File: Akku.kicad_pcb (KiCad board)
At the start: 2 copper layers, 100 x 160 mm, 34 parts, among them P1 CONN_02X10, P2 CONN_02X10, P3 CONN_02X10, SW1 SWITCH_INV, SW2 SWITCH_INV, SW3 SWITCH_INV, U4 74LS193, U5 74LS541, U6 74LS193, U7 74LS540

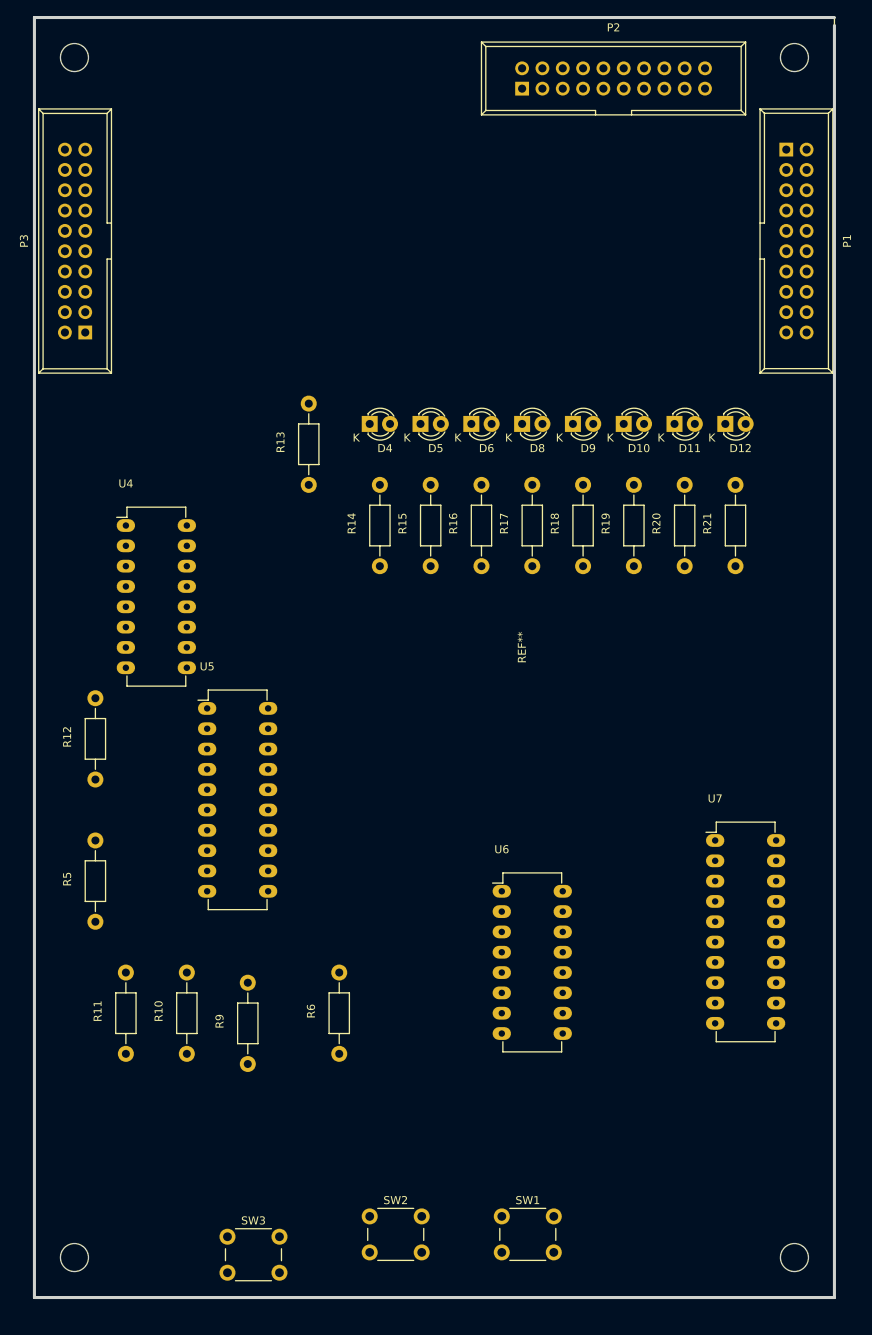
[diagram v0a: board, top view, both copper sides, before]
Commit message: Akku/PC PCB verbessert
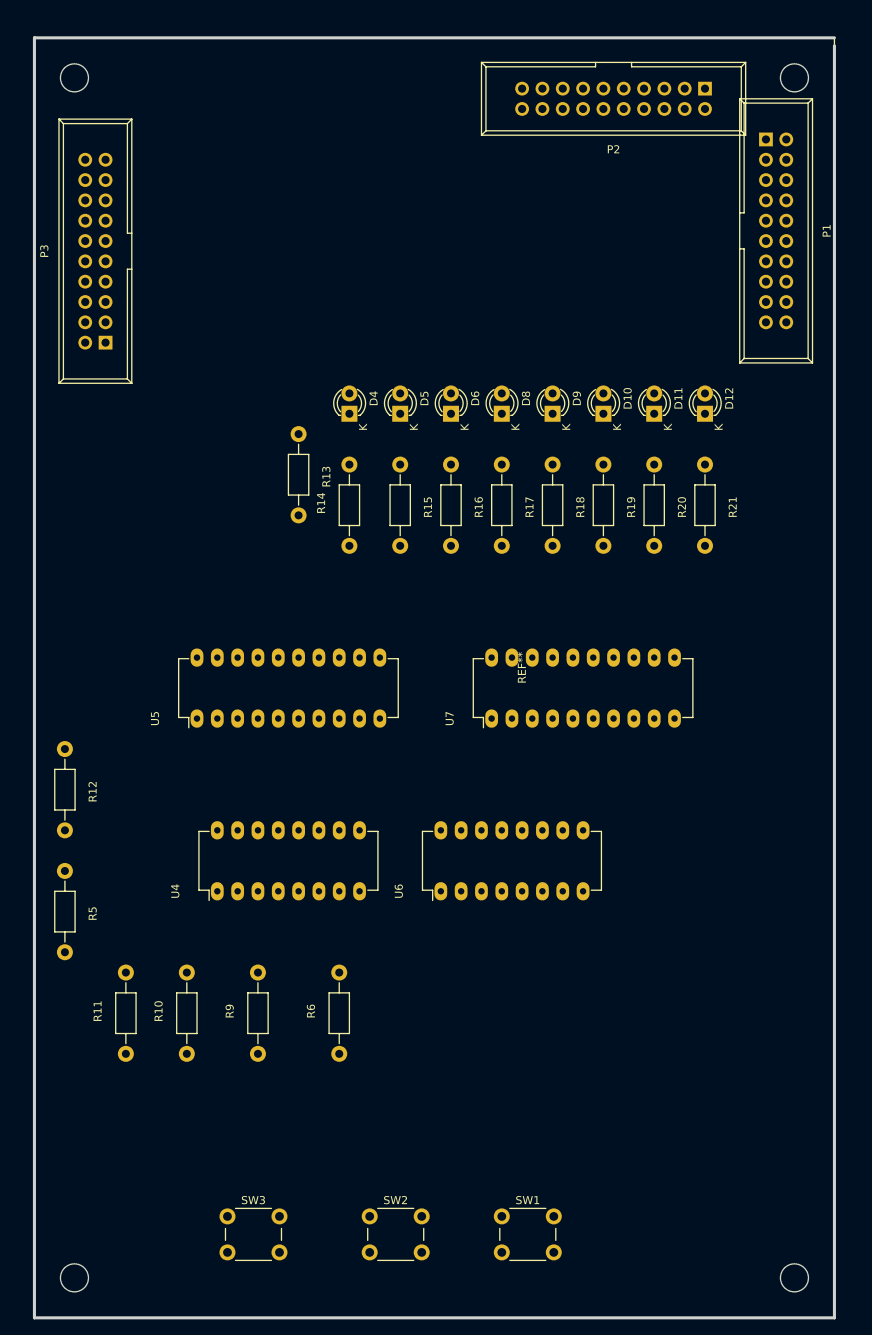
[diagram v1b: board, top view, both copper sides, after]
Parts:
- moved U4 47.1 mm to (73.7, 163.8), turned to 90 degrees
- moved U7 31.8 mm to (108.0, 142.2), turned to 90 degrees
- moved P2 22.9 mm to (134.6, 63.5), turned to 180 degrees
- moved R15 13.3 mm to (96.5, 110.5), turned to 270 degrees
- moved R16 13.3 mm to (102.9, 110.5), turned to 270 degrees
- moved R17 13.3 mm to (109.2, 110.5), turned to 270 degrees
- moved R18 13.3 mm to (115.6, 110.5), turned to 270 degrees
- moved R19 13.3 mm to (121.9, 110.5), turned to 270 degrees
- moved R20 13.3 mm to (128.3, 110.5), turned to 270 degrees
- moved R21 13.3 mm to (134.6, 110.5), turned to 270 degrees
- moved U6 7.62 mm to (101.6, 163.8), turned to 90 degrees
- moved R5 7.41 mm to (54.6, 161.3), turned to 270 degrees
- moved R13 6.48 mm to (83.8, 106.7), turned to 270 degrees
- moved R12 5.39 mm to (54.6, 146.1), turned to 270 degrees
- moved R14 4.58 mm to (90.2, 120.7)
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
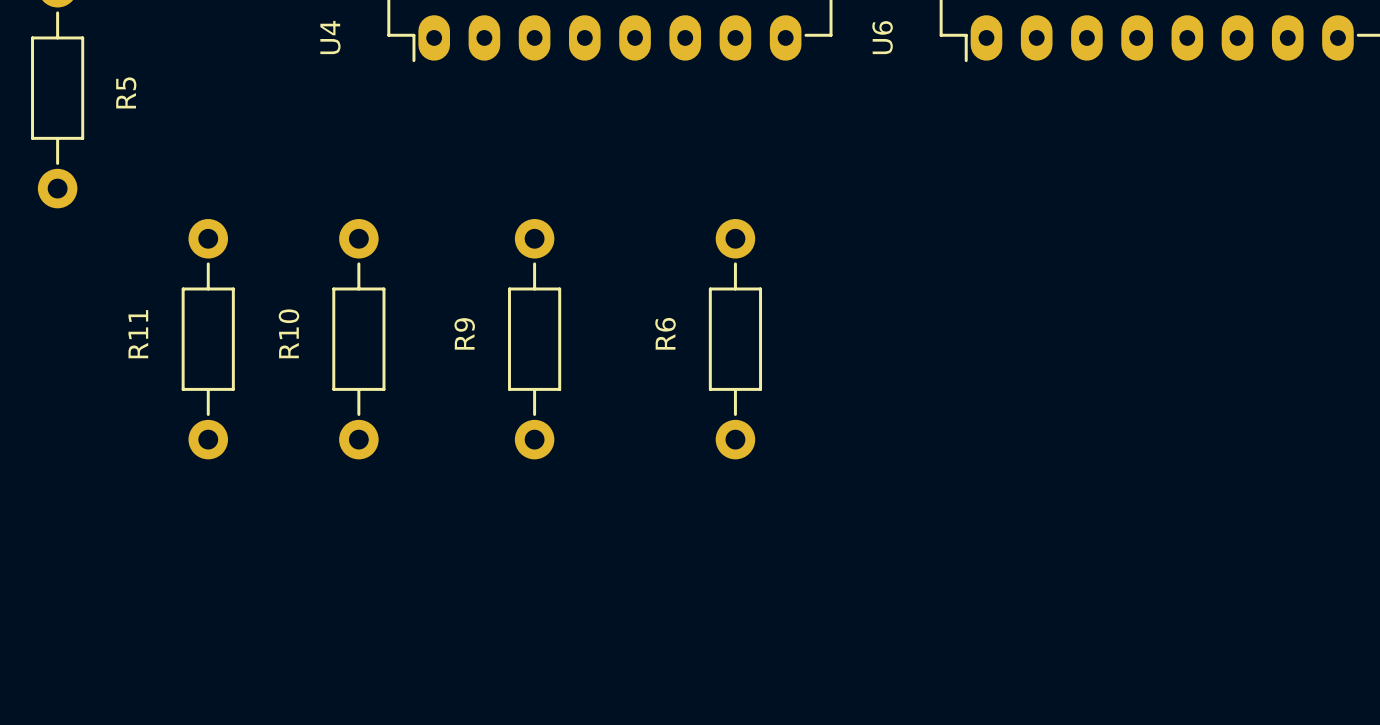
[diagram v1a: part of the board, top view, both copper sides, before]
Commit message: Fehler am Schaltplan ausgebessert; PCB erweitert
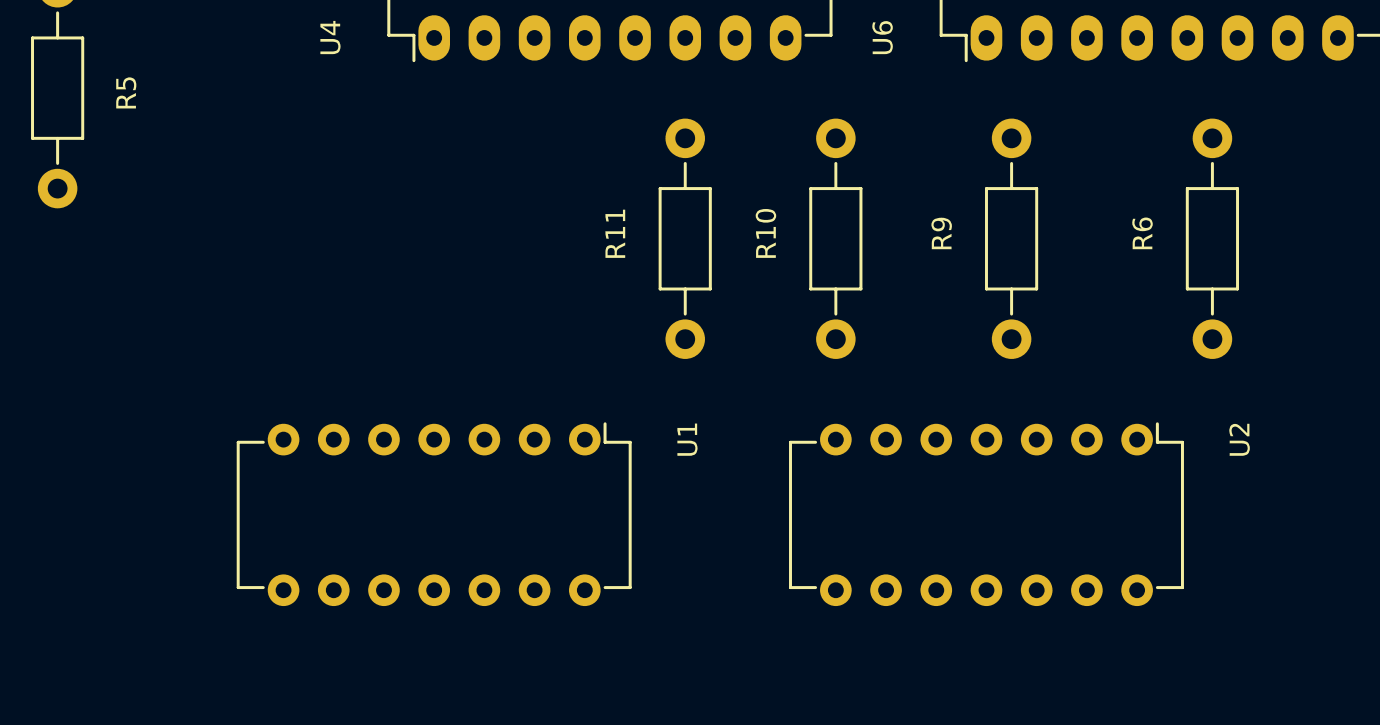
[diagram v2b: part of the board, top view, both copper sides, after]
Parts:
- added U1: 7400, Housings_DIP:DIP-14_W7.62mm, F.Cu at (81.3, 184.2)
- added U2: 7408, Housings_DIP:DIP-14_W7.62mm, F.Cu at (109.2, 184.2)
- moved R10 24.7 mm to (94.0, 179.1)
- moved R9 24.7 mm to (102.9, 179.1)
- moved R11 24.7 mm to (86.4, 179.1)
- moved R6 24.7 mm to (113.0, 179.1)

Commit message: netzlisten neu
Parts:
- moved P1 28.2 mm to (146.1, 97.8), turned to 90 degrees
- moved P2 25.5 mm to (109.2, 66.0), turned to 0 degrees
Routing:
- net Net-(P1-Pad1): track 0.00 -> 27.9 mm
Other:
- net class Dicke Leitung added: clearance 0.2, trace_width 0.5, via_dia 0.6, via_drill 0.4
